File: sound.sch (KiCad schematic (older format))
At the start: 18 parts, among them IC1 MAX4466EXK+T

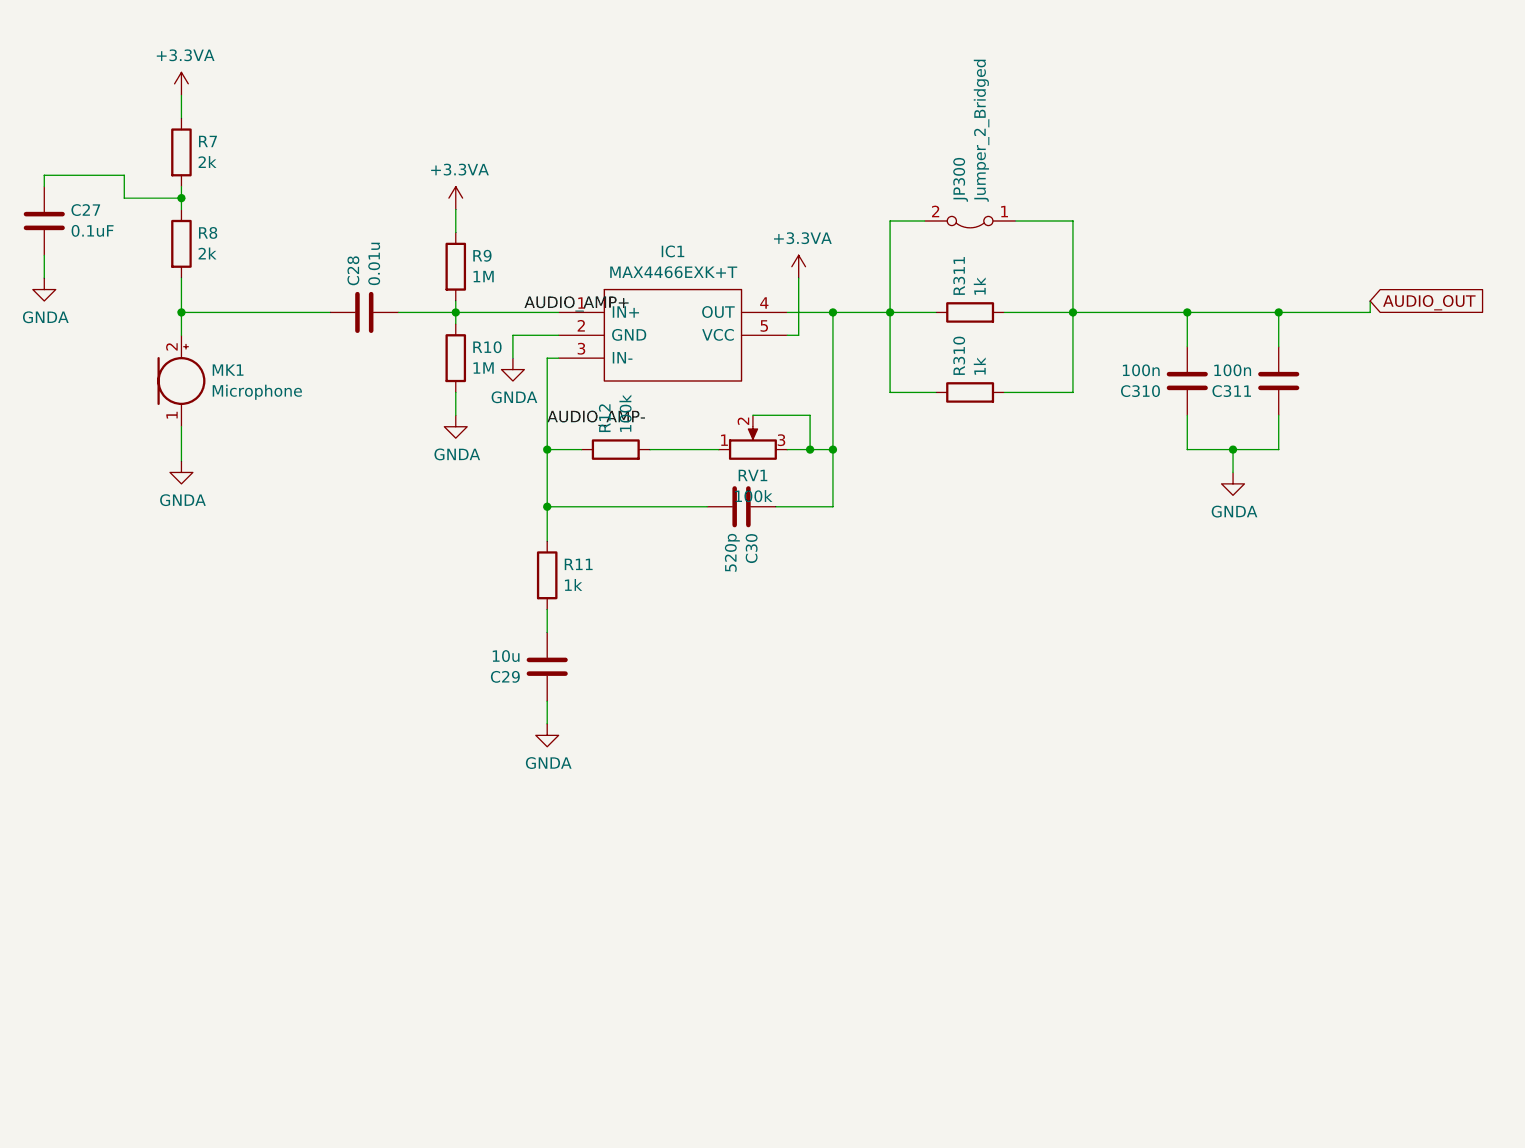
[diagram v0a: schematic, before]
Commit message: Added some primitive filter for 3V3A and GNDA. Added the IMU to the board.
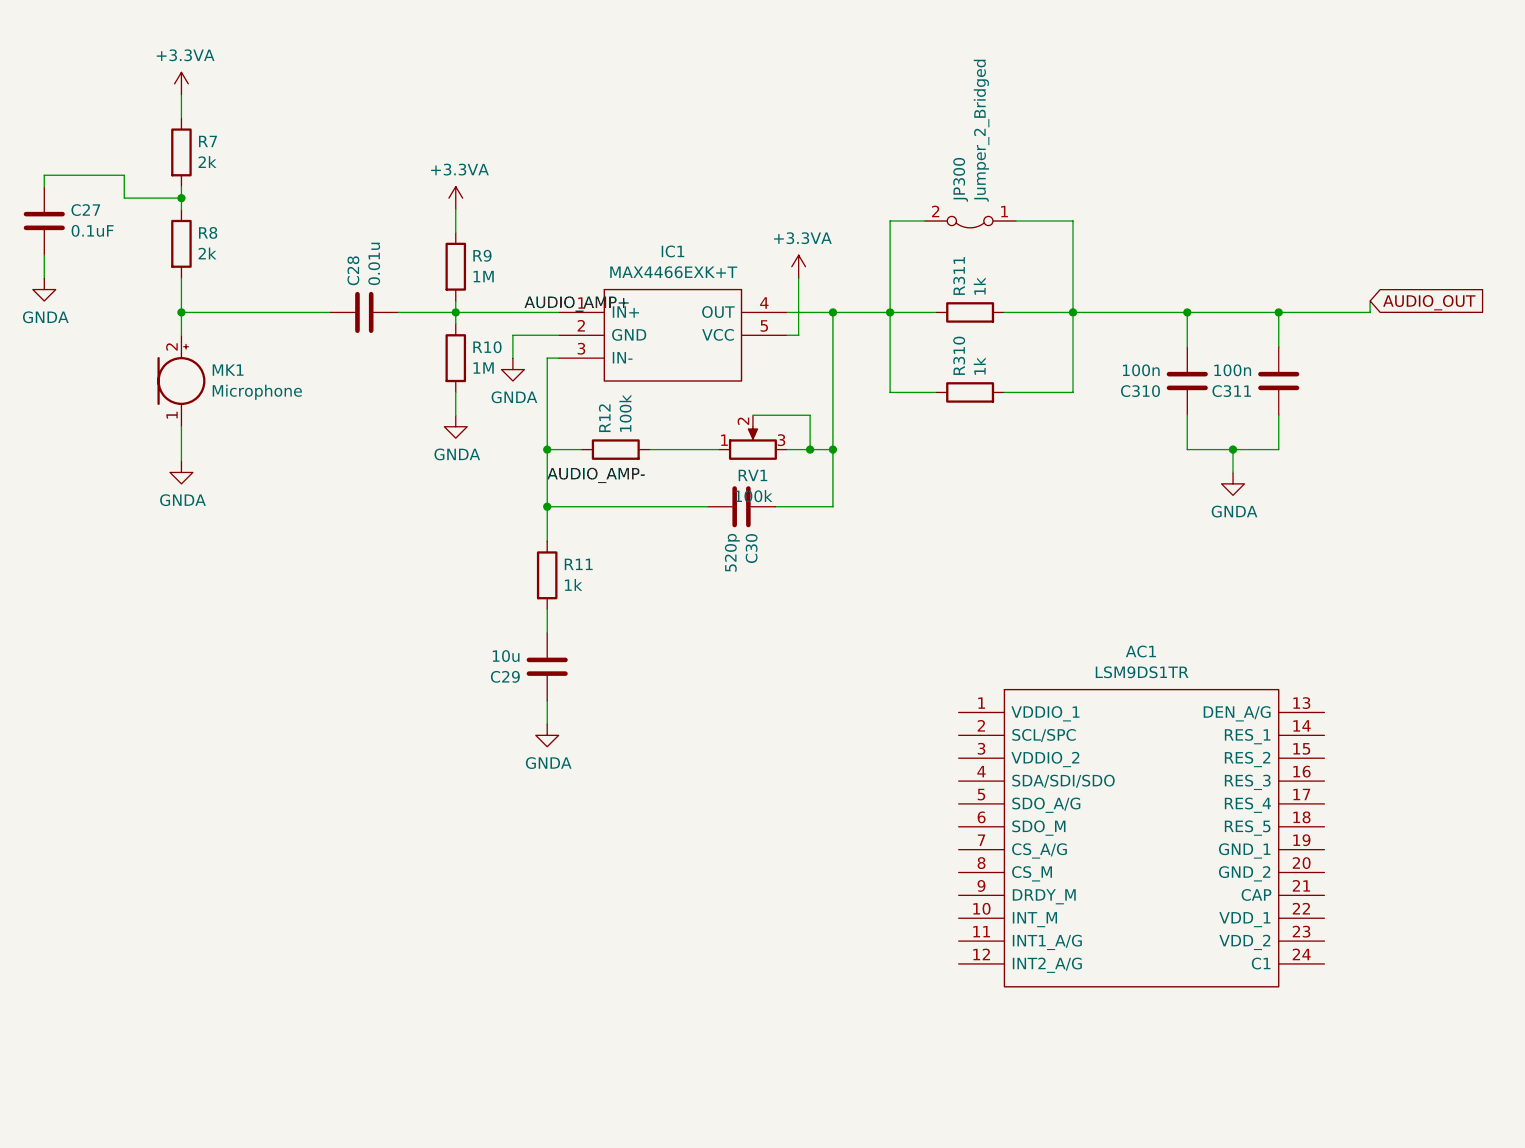
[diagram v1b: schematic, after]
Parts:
- added AC1: LSM9DS1TR, Special_Parts:LGA-24L_3X3.5X1MM_, symbol Special_Parts:LSM9DS1TR
- MK1: footprint SamacSys_Parts:CMEJ062742P -> Special_Parts:CMEJ062742P
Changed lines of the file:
@@
 F 0 "MK1" H 2030 2396 50  0000 L CNN
 F 1 "Microphone" H 2030 2305 50  0000 L CNN
-F 2 "SamacSys_Parts:CMEJ062742P" V 1900 2450 50  0001 C CNN
+F 2 "Special_Parts:CMEJ062742P" V 1900 2450 50  0001 C CNN
 F 3 "~" V 1900 2450 50  0001 C CNN
 	1    1900 2350
@@
 Wire Wire Line
 	4750 2650 4750 2900
-Text Label 3500 2550 0    50   ~ 0
+Text Label 3500 2800 0    50   ~ 0
 AUDIO_AMP-
 Text Label 3400 2050 0    50   ~ 0
@@
 P 6500 2750
 AR Path="/615D7A24" Ref="#PWR?"  Part="1"
-AR Path="/6099554C/615D7A24" Ref="#PWR?"  Part="1"
-F 0 "#PWR?" H 6500 2500 50  0001 C CNN
+AR Path="/6099554C/615D7A24" Ref="#PWR0123"  Part="1"
+F 0 "#PWR0123" H 6500 2500 50  0001 C CNN
 F 1 "GNDA" H 6505 2577 50  0000 C CNN
 F 2 "" H 6500 2750 50  0001 C CNN
@@
 Wire Wire Line
 	6500 2650 6700 2650
+$Comp
+L Special_Parts:LSM9DS1TR AC1
+U 1 1 615C84F5
+P 5300 3800
+F 0 "AC1" H 6100 4065 50  0000 C CNN
+F 1 "LSM9DS1TR" H 6100 3974 50  0000 C CNN
+F 2 "Special_Parts:LGA-24L_3X3.5X1MM_" H 6750 3900 50  0001 L CNN
+F 3 "http://www.st.com/content/ccc/resource/technical/document/datasheet/1e/3f/2a/d6/25/eb/48/46/DM00103319.pdf/files/DM00103319.pdf/jcr:content/translations/en.DM00103319.pdf" H 6750 3800 50  0001 L CNN
+F 4 "iNEMO Inertial 3D Accel/Gyro/Magn. LGA24 STMicroelectronics LSM9DS1TR 3-Axis Accelerometer, Gyroscope & Magnetometer, 0  400 kHz, 1.9  3.6 V" H 6750 3700 50  0001 L CNN "Description"
+F 5 "511-LSM9DS1TR" H 6750 3500 50  0001 L CNN "Mouser Part Number"
+F 6 "https://www.mouser.co.uk/ProductDetail/STMicroelectronics/LSM9DS1TR?qs=4b8myOmUP%252BsiwRDrJOMxKQ%3D%3D" H 6750 3400 50  0001 L CNN "Mouser Price/Stock"
+F 7 "STMicroelectronics" H 6750 3300 50  0001 L CNN "Manufacturer_Name"
+F 8 "LSM9DS1TR" H 6750 3200 50  0001 L CNN "Manufacturer_Part_Number"
+	1    5300 3800
+	1    0    0    -1
+$EndComp
 $EndSCHEMATC

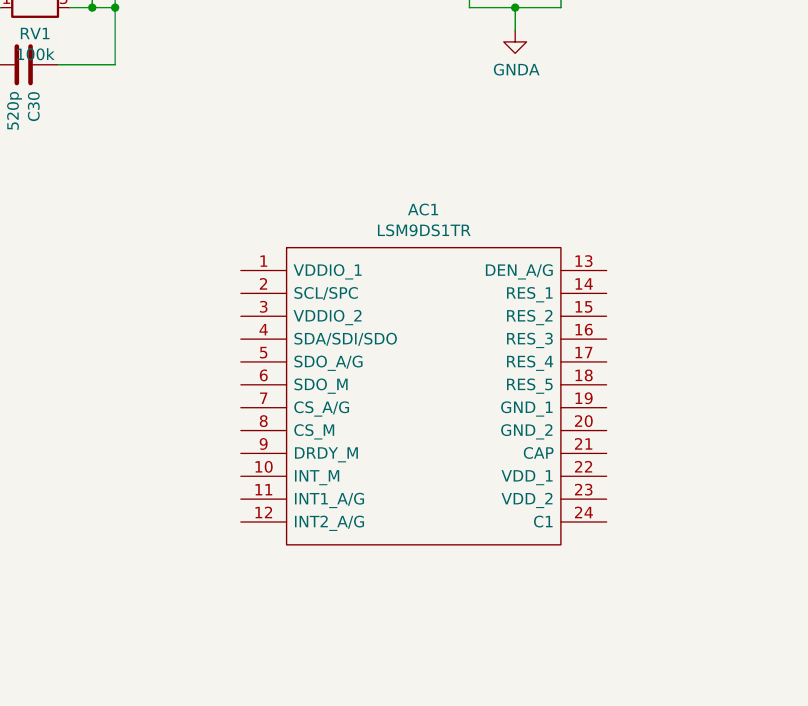
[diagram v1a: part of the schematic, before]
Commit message: Updated to kicad 6. Added AMS1117 regulator. Did more layout work in power section.
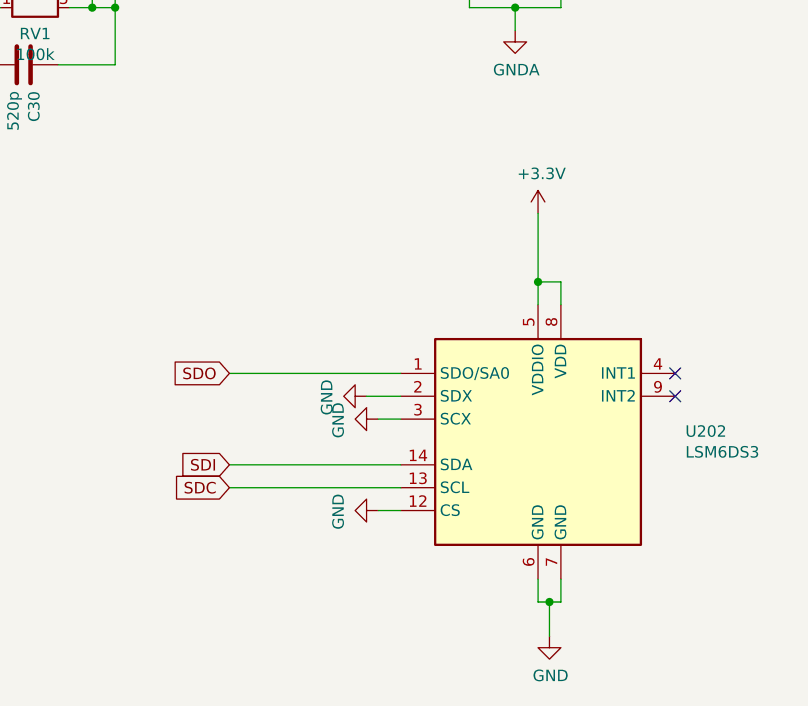
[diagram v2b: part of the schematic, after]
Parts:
- removed AC1: LSM9DS1TR, Special_Parts:LGA-24L_3X3.5X1MM_, symbol Special_Parts:LSM9DS1TR
- added U202: LSM6DS3, Package_LGA:LGA-14_3x2.5mm_P0.5mm_LayoutBorder3x4y, symbol Sensor_Motion:LSM6DS3
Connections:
- new net +3V3: U202.5 (VDDIO), U202.8 (VDD)
- new net GND: U202.12 (CS), U202.2 (SDX), U202.3 (SCX), U202.6 (GND), U202.7 (GND)
- new net SDC: U202.13 (SCL)
- new net SDI: U202.14 (SDA)
- new net SDO: U202.1 (SDO/SA0)
- no-connect marks 0 -> 2
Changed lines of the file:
@@
 	6500 2650 6700 2650
 $Comp
-L Special_Parts:LSM9DS1TR AC1
-U 1 1 615C84F5
-P 5300 3800
-F 0 "AC1" H 6100 4065 50  0000 C CNN
-F 1 "LSM9DS1TR" H 6100 3974 50  0000 C CNN
-F 2 "Special_Parts:LGA-24L_3X3.5X1MM_" H 6750 3900 50  0001 L CNN
-F 3 "http://www.st.com/content/ccc/resource/technical/document/datasheet/1e/3f/2a/d6/25/eb/48/46/DM00103319.pdf/files/DM00103319.pdf/jcr:content/translations/en.DM00103319.pdf" H 6750 3800 50  0001 L CNN
-F 4 "iNEMO Inertial 3D Accel/Gyro/Magn. LGA24 STMicroelectronics LSM9DS1TR 3-Axis Accelerometer, Gyroscope & Magnetometer, 0  400 kHz, 1.9  3.6 V" H 6750 3700 50  0001 L CNN "Description"
-F 5 "511-LSM9DS1TR" H 6750 3500 50  0001 L CNN "Mouser Part Number"
-F 6 "https://www.mouser.co.uk/ProductDetail/STMicroelectronics/LSM9DS1TR?qs=4b8myOmUP%252BsiwRDrJOMxKQ%3D%3D" H 6750 3400 50  0001 L CNN "Mouser Price/Stock"
-F 7 "STMicroelectronics" H 6750 3300 50  0001 L CNN "Manufacturer_Name"
-F 8 "LSM9DS1TR" H 6750 3200 50  0001 L CNN "Manufacturer_Part_Number"
-	1    5300 3800
+L power:GND #PWR?
+U 1 1 61B361F4
+P 6650 5400
+AR Path="/609974E9/61B361F4" Ref="#PWR?"  Part="1"
+AR Path="/6099554C/61B361F4" Ref="#PWR0124"  Part="1"
+F 0 "#PWR0124" H 6650 5150 50  0001 C CNN
+F 1 "GND" H 6655 5227 50  0000 C CNN
+F 2 "" H 6650 5400 50  0001 C CNN
+F 3 "" H 6650 5400 50  0001 C CNN
+	1    6650 5400
 	1    0    0    -1
 $EndComp
+$Comp
+L power:+3.3V #PWR?
+U 1 1 61B386C1
+P 6600 3550
+AR Path="/609974E9/61B386C1" Ref="#PWR?"  Part="1"
+AR Path="/6099554C/61B386C1" Ref="#PWR0125"  Part="1"
+F 0 "#PWR0125" H 6600 3400 50  0001 C CNN
+F 1 "+3.3V" H 6615 3723 50  0000 C CNN
+F 2 "" H 6600 3550 50  0001 C CNN
+F 3 "" H 6600 3550 50  0001 C CNN
+	1    6600 3550
+	1    0    0    -1
+$EndComp
+Wire Wire Line
+	6600 3550 6600 3850
+Wire Wire Line
+	6700 3950 6700 3850
+Wire Wire Line
+	6700 3850 6600 3850
+Connection ~ 6600 3850
+Wire Wire Line
+	6600 3850 6600 3950
+Wire Wire Line
+	6650 5400 6650 5250
+Wire Wire Line
+	6650 5250 6600 5250
+Wire Wire Line
+	6600 5250 6600 5150
+Wire Wire Line
+	6700 5150 6700 5250
+Wire Wire Line
+	6700 5250 6650 5250
+Connection ~ 6650 5250
+$Comp
+L power:GND #PWR?
+U 1 1 61B3EEF1
+P 5900 4450
+AR Path="/609974E9/61B3EEF1" Ref="#PWR?"  Part="1"
+AR Path="/6099554C/61B3EEF1" Ref="#PWR0126"  Part="1"
+F 0 "#PWR0126" H 5900 4200 50  0001 C CNN
+F 1 "GND" H 5905 4277 50  0000 C CNN
+F 2 "" H 5900 4450 50  0001 C CNN
+F 3 "" H 5900 4450 50  0001 C CNN
+	1    5900 4450
+	0    1    1    0
+$EndComp
+Wire Wire Line
+	5900 4450 6000 4450
+$Comp
+L power:GND #PWR?
+U 1 1 61B400C0
+P 5850 4350
+AR Path="/609974E9/61B400C0" Ref="#PWR?"  Part="1"
+AR Path="/6099554C/61B400C0" Ref="#PWR0127"  Part="1"
+F 0 "#PWR0127" H 5850 4100 50  0001 C CNN
+F 1 "GND" H 5855 4177 50  0000 C CNN
+F 2 "" H 5850 4350 50  0001 C CNN
+F 3 "" H 5850 4350 50  0001 C CNN
+	1    5850 4350
+	0    1    1    0
+$EndComp
+Wire Wire Line
+	5850 4350 6000 4350
+$Comp
+L Sensor_Motion:LSM6DS3 U202
+U 1 1 61B29B38
+P 6600 4550
+F 0 "U202" H 7244 4596 50  0000 L CNN
+F 1 "LSM6DS3" H 7244 4505 50  0000 L CNN
+F 2 "Package_LGA:LGA-14_3x2.5mm_P0.5mm_LayoutBorder3x4y" H 6200 3850 50  0001 L CNN
+F 3 "www.st.com/resource/en/datasheet/lsm6ds3.pdf" H 6700 3900 50  0001 C CNN
+	1    6600 4550
+	1    0    0    -1
+$EndComp
+Wire Wire Line
+	5250 4250 6000 4250
+$Comp
+L power:GND #PWR?
+U 1 1 61B458D5
+P 5900 4850
+AR Path="/609974E9/61B458D5" Ref="#PWR?"  Part="1"
+AR Path="/6099554C/61B458D5" Ref="#PWR0128"  Part="1"
+F 0 "#PWR0128" H 5900 4600 50  0001 C CNN
+F 1 "GND" H 5905 4677 50  0000 C CNN
+F 2 "" H 5900 4850 50  0001 C CNN
+F 3 "" H 5900 4850 50  0001 C CNN
+	1    5900 4850
+	0    1    1    0
+$EndComp
+Wire Wire Line
+	5900 4850 6000 4850
+Wire Wire Line
+	5250 4650 6000 4650
+Wire Wire Line
+	5250 4750 6000 4750
+NoConn ~ 7200 4350
+NoConn ~ 7200 4250
+Text GLabel 5250 4250 0    50   Input ~ 0
+SDO
+Text GLabel 5250 4750 0    50   Input ~ 0
+SDC
+Text GLabel 5250 4650 0    50   Input ~ 0
+SDI
 $EndSCHEMATC
